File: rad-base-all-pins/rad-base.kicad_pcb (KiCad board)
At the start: 4 copper layers, 43.2 x 43.2 mm, 167 parts, among them U1 S1D13513F01A100

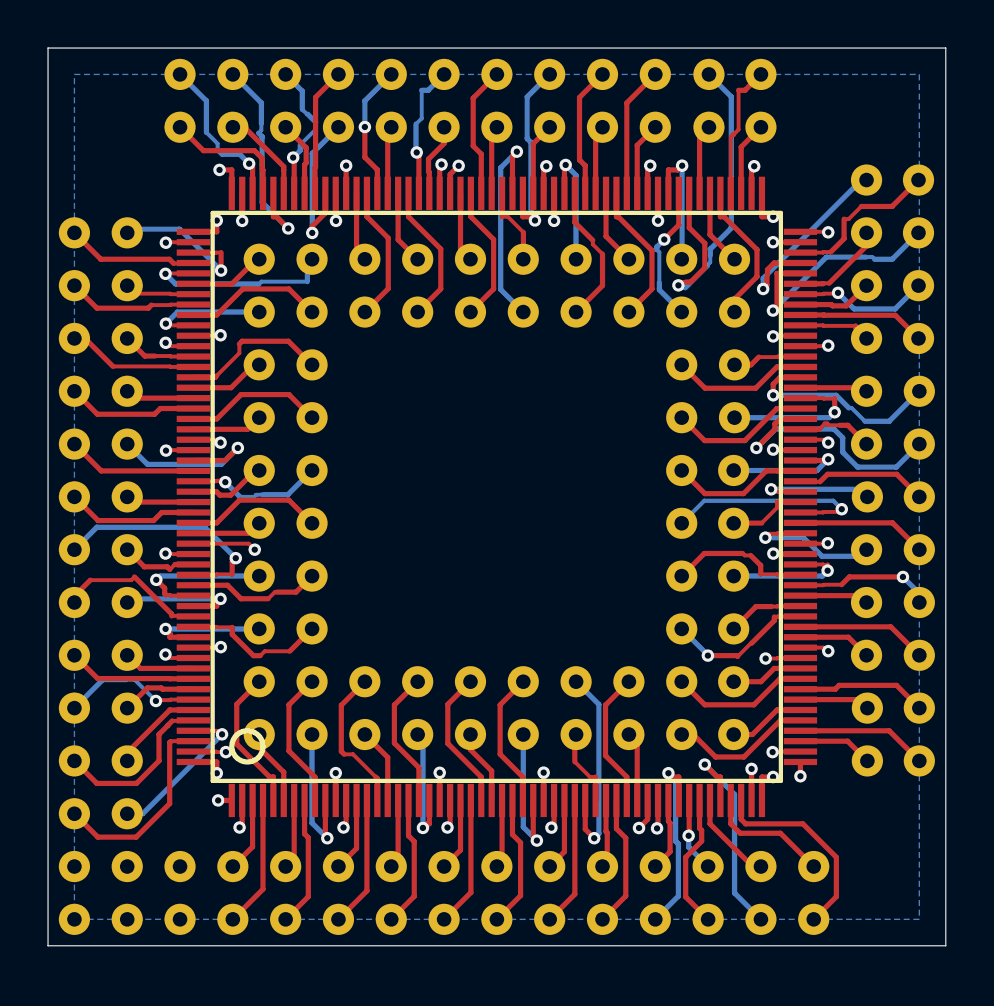
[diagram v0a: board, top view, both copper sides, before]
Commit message: Expanded pads and increased font size
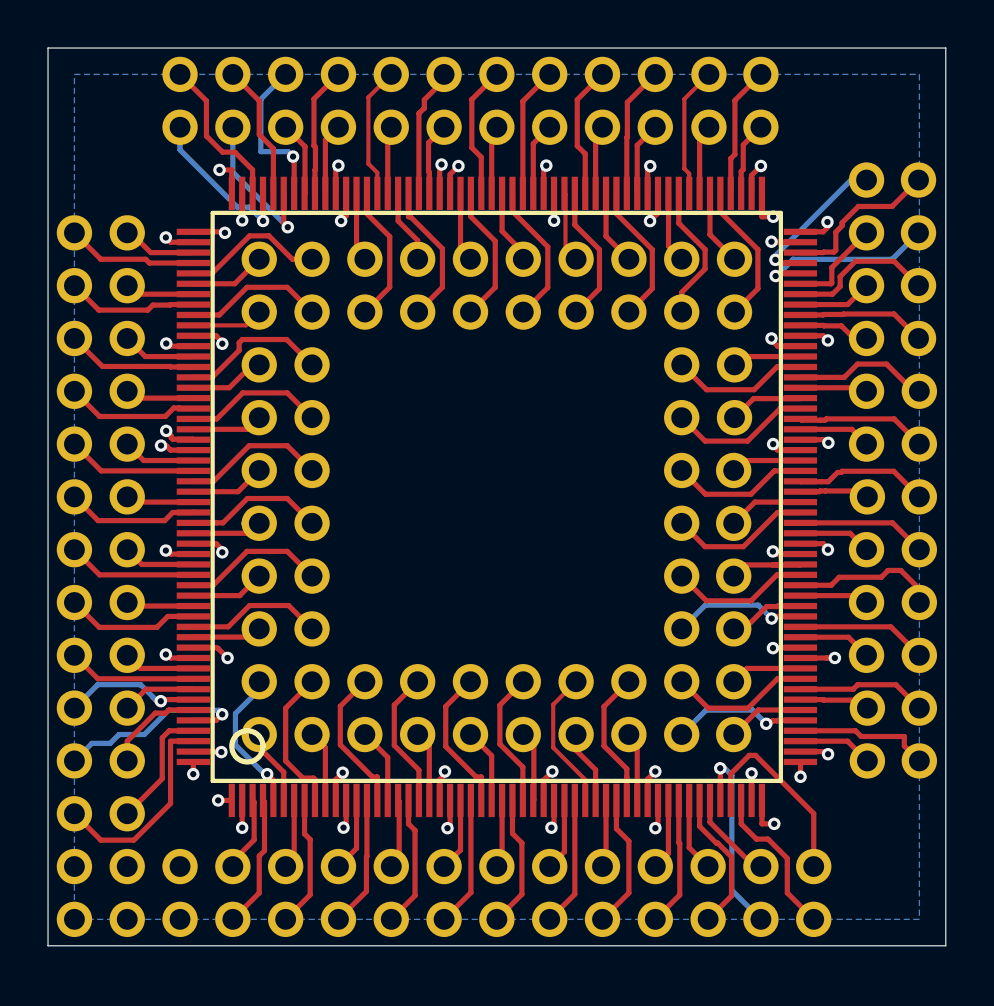
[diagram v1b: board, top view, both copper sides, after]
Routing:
- net w86: track 17.6 -> 6.31 mm, vias 1 -> 0
- net w66: track 12.7 -> 6.27 mm, vias 1 -> 0
- net w146: track 11.6 -> 6.22 mm, vias 1 -> 0
- net w137: track 8.44 -> 3.51 mm, vias 1 -> 0
- net w113: track 7.77 -> 3.44 mm, vias 1 -> 0
- net w118: track 10.7 -> 6.53 mm, vias 1 -> 0
- net w121: track 7.61 -> 3.57 mm, vias 1 -> 0
- net w24: track 7.38 -> 3.39 mm, vias 1 -> 0
- net w148: track 7.28 -> 3.56 mm, vias 1 -> 0
- net w8: track 7.15 -> 3.44 mm, vias 1 -> 0
- net w68: track 7.24 -> 3.56 mm, vias 1 -> 0
- net w99: track 10.6 -> 6.90 mm, vias 1 -> 0
- net w70: track 10.1 -> 6.53 mm, vias 1 -> 0
- net w59: track 10.4 -> 6.86 mm, vias 1 -> 0
- net w39: track 5.97 -> 9.34 mm
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
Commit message: Changed footprint to IC149-208-161-B5
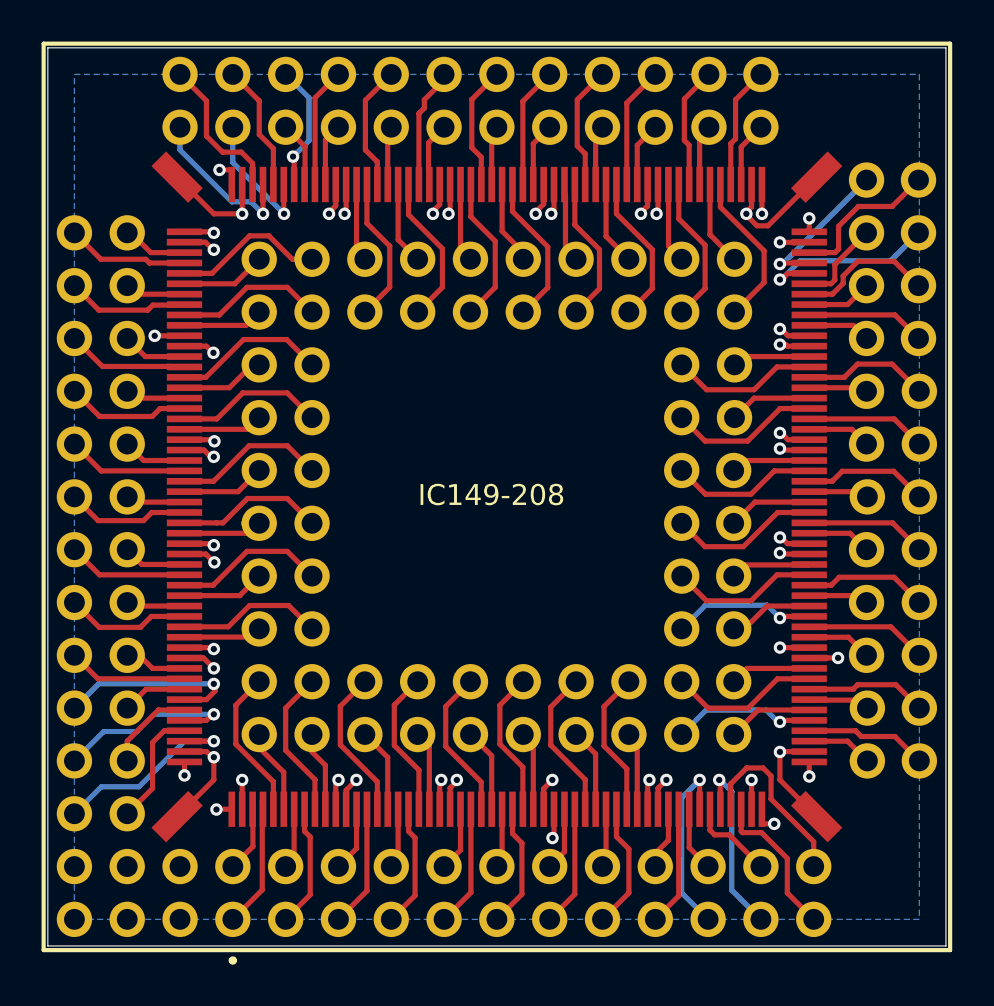
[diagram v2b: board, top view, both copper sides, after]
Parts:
- removed U1: S1D13513F01A100, S1D13513F01A100:QFP208-28X28MM
- added J1: IC149-208-161-B5, IC149-208-161-B5:IC149208061B5, F.Cu at (137.2, 99.1)
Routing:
- net GND: track 34.9 -> 44.3 mm
- net VCC1: track 15.9 -> 12.8 mm
- net w36: track 6.86 -> 9.05 mm, vias 0 -> 1
- net w156: track 6.83 -> 8.80 mm
- net VCC2: track 17.5 -> 16.0 mm
- net w117: track 7.61 -> 6.18 mm
- net w116: track 7.64 -> 6.53 mm
- net w39: track 9.34 -> 8.42 mm
- net w158: track 9.73 -> 8.84 mm
- net w56: track 3.44 -> 4.29 mm
- net w160: track 9.97 -> 9.18 mm, vias 0 -> 1
- net w38: track 9.75 -> 9.00 mm
- net w54: track 7.04 -> 6.38 mm
- net w27: track 6.80 -> 7.33 mm
- net w3: track 7.01 -> 7.30 mm, vias 1 -> 0
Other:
- board text added: "IC149-208"
